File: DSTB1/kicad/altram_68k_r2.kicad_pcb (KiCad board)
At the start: 2 copper layers, 28.2 x 82 mm, 37 parts, among them IC1 IS42S16320D-7TL, IC2 SN74CB3T3245PW, IC3 SN74CB3T3245PW, J1 Conn_01x06_Male, U1 68000D, U2 68000D, U3 XC95144XL-TQ100, U4 LT1129-3.3_SOT223, X1 IQXO-70

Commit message: Working on the refactor for rev2
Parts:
- removed JP1: SolderJumper_3_Open, Jumper:SolderJumper-3_P1.3mm_Open_RoundedPad1.0x1.5mm
- removed RN11: 3k3, Resistor_SMD:R_Array_Convex_4x0603
- added R3: 2k2, Resistor_SMD:R_0805_2012Metric_Pad1.20x1.40mm_HandSolder, B.Cu at (144.7, 130.1)
- J1: value Conn_01x06_Male -> Conn_01x06_Pin
- R1: value R -> 1k
- TP1, TP2: value TestPoint -> (none)
- moved C5 13.1 mm to (148.2, 93.1), turned to 90 degrees
- moved R1 4.51 mm to (146.2, 127.3), turned to -90 degrees
- moved D1 3.54 mm to (149.6, 130.7), turned to 180 degrees
- moved U1 2.54 mm to (134.1, 55.6)
- moved U2 2.54 mm to (131.6, 55.6)
- moved TP1 0.15 mm to (141.7, 130.1), turned to 0 degrees
- turned TP2 to 0 degrees
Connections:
- net /TP1 renamed /TOS206
- net R~W renamed R~{W}
- net ~AS renamed ~{AS}
- net ~AS_INT renamed ~{AS_INT}
- net ~BERR renamed ~{BERR}
- net ~BOE renamed ~{BOE}
- net ~CAS renamed ~{CAS}
- net ~DTACK renamed ~{DTACK}
- net ~DTACK_INT renamed ~{DTACK_INT}
- net ~HLT renamed ~{HLT}
- net ~LDS renamed ~{LDS}
- net ~RAMWE renamed ~{RAMWE}
- net ~RAS renamed ~{RAS}
- net ~RST renamed ~{RST}
- net ~UDS renamed ~{UDS}
- net ~VMA renamed ~{VMA}
- net ~VMA_INT renamed ~{VMA_INT}
- net ~VPA renamed ~{VPA}
- C7 pad 1: Net-(C7-Pad1) -> VCC3
- IC1 pad 37: VCC3 -> CKE
- IC1 pad 38: RAMCLK -> OSC
- IC1 pad 40: Net-(IC1-Pad40) -> unconnected-(IC1-NC-Pad40)
- IC2 pad 1: Net-(IC2-Pad1) -> unconnected-(IC2-NC-Pad1)
- IC3 pad 1: Net-(IC3-Pad1) -> unconnected-(IC3-NC-Pad1)
- RN10 pad 5: Net-(RN10-Pad5) -> unconnected-(RN10-R4.2-Pad5)
- U1 pad 11: BG -> BGO
- U2 pad 11: BG -> BGI
- U3 pad 15: Net-(U3-Pad15) -> unconnected-(U3-P15-Pad15)
- U3 pad 16: Net-(U3-Pad16) -> unconnected-(U3-P16-Pad16)
- U3 pad 24: Net-(U3-Pad24) -> unconnected-(U3-P24-Pad24)
- U3 pad 25: Net-(U3-Pad25) -> unconnected-(U3-P25-Pad25)
- U3 pad 27: RAMCLK -> OSC
- U3 pad 36: OSC -> unconnected-(U3-P36-Pad36)
- U3 pad 54: /TP4 -> BGO
- U3 pad 55: /TP5 -> BGI
- U3 pad 58: Net-(U3-Pad58) -> /TP4
- U3 pad 59: Net-(U3-Pad59) -> /TP5
- U3 pad 60: Net-(U3-Pad60) -> /TP3
- U3 pad 61: Net-(U3-Pad61) -> unconnected-(U3-P61-Pad61)
- U3 pad 65: Net-(U3-Pad65) -> unconnected-(U3-P65-Pad65)
- U3 pad 66: /TP3 -> CKE
- X1 pad 1: Net-(X1-Pad1) -> unconnected-(X1-E/B-Pad1)
- X1 pad 4: Net-(C7-Pad1) -> VCC3
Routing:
- net BGI: track 0.00 -> 46.3 mm, vias 0 -> 1
- net BGO: track 0.00 -> 42.8 mm, vias 0 -> 1
- net OSC: track 13.3 -> 52.5 mm, vias 2 -> 3
- net RAMCLK: track 38.6 -> 0.00 mm, vias 2 -> 0
- net CKE: track 0.00 -> 24.1 mm, vias 0 -> 2
- net VCC: track 212.9 -> 195.4 mm, vias 6 -> 4
- net VCC3: track 188.4 -> 173.2 mm
- net Net-(C7-Pad1): track 8.72 -> 0.00 mm, vias 1 -> 0
- net /TP3: track 37.2 -> 29.7 mm, vias 2 -> 1
- net Net-(D1-A): track 10.2 -> 3.28 mm
- net ~{DTACK_INT}: track 31.4 -> 37.1 mm
- net /TP2: track 33.0 -> 27.8 mm, vias 2 -> 1
- net ~{VMA_INT}: track 3.21 -> 7.67 mm
- net E_INT: track 3.02 -> 7.16 mm
- net E: track 5.76 -> 3.22 mm
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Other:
- net class CLK removed
- net class Default removed
- net class PWR removed
- board text added: "David’s ST Booster mk 1, DSTB1r2 Copyright 2021-4 D Henderson Released under the terms of the GPLv2 https://github.com/dh219/DSTB"
- board text added: "FRAME"
- board text added: "TOS206"
- board text added: "~{DSTB1}r2"
- board text removed: "David’s ST Booster mk 1, DSTB1r1 Copyright 2021-2 D Henderson & others Released under the terms of the GPLv2 https://github.com/dh219/DSTB"
- board text removed: "~DSTB1"

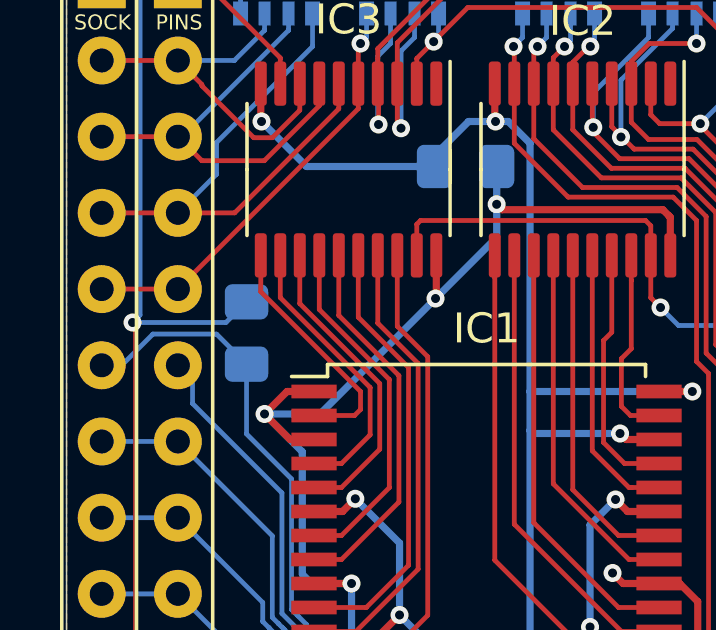
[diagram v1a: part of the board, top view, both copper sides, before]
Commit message: No DRC fails. All symbols updated. Bit of ground stitching.
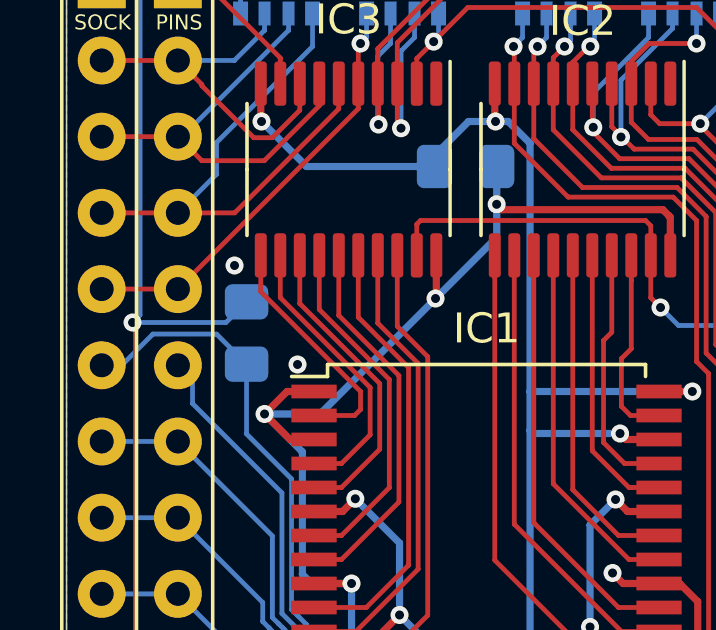
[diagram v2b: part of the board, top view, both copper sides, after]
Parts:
- TP1: value (none) -> TOS206
- TP2: value (none) -> FRAME
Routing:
- net GND: vias 27 -> 29
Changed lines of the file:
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@@
 			)
 		)
-		(property "Description" ""
+		(property "Description" "CPLD, 144 Macrocells, 3200 Usable Gates"
 			(at 0 0 0)
 			(layer "F.Fab")
@@
 			)
 		)
-		(property "Description" ""
+		(property "Description" "16/32-bit Microprocessor"
 			(at 0 0 0)
 			(layer "F.Fab")
@@
 			)
 		)
+		(property "Description_1" "Texas Instruments SN74CB3T3245DW, Bus Switch, 8 x 1:1, 2.3  3.6 V, 20-Pin SOIC"
+			(at 0 0 -90)
+			(unlocked yes)
+			(layer "F.Fab")
+			(hide yes)
+			(effects
+				(font
+					(size 1 1)
+					(thickness 0.15)
+				)
+			)
+		)
 		(sheetname "Root")
 		(sheetfile "altram_68k_r2.kicad_sch")
@@
 			)
 		)
+		(property "Description_1" "Texas Instruments SN74CB3T3245DW, Bus Switch, 8 x 1:1, 2.3  3.6 V, 20-Pin SOIC"
+			(at 0 0 -90)
+			(unlocked yes)
+			(layer "F.Fab")
+			(hide yes)
+			(effects
+				(font
+					(size 1 1)
+					(thickness 0.15)
+				)
+			)
+		)
 		(sheetname "Root")
 		(sheetfile "altram_68k_r2.kicad_sch")
@@
 			)
 		)
-		(property "Description" ""
+		(property "Description" "test point"
 			(at 0 0 90)
 			(layer "F.Fab")
@@
 			)
 		)
-		(property "Description" ""
+		(property "Description" "Crystal Clock Oscillator, SMD package 7.5x5.0mm²"
 			(at 0 0 -90)
 			(layer "F.Fab")
@@
 			)
 		)
-		(property "Description" ""
+		(property "Description" "test point"
 			(at 0 0 -90)
 			(layer "F.Fab")
@@
 			)
 		)
-		(property "Description" ""
+		(property "Description" "test point"
 			(at 0 0 -90)
 			(layer "F.Fab")
@@
 		(tags "LED handsolder")
 		(property "Reference" "D1"
-			(at 0 1.65 360)
+			(at 0 1.65 0)
 			(layer "F.SilkS")
 			(effects
@@
 		)
 		(property "Value" "LED"
-			(at 0 1.65 360)
+			(at 0 1.65 0)
 			(layer "F.Fab")
 			(effects
@@
 		)
 		(property "Footprint" "LED_SMD:LED_0805_2012Metric_Pad1.15x1.40mm_HandSolder"
-			(at 0 0 360)
+			(at 0 0 0)
 			(layer "F.Fab")
 			(hide yes)
@@
 		)
 		(property "Datasheet" ""
-			(at 0 0 360)
+			(at 0 0 0)
 			(layer "F.Fab")
 			(hide yes)
@@
 			)
 		)
-		(property "Description" ""
-			(at 0 0 360)
+		(property "Description" "Light emitting diode"
+			(at 0 0 0)
 			(layer "F.Fab")
 			(hide yes)
@@
 		)
 		(fp_text user "${REFERENCE}"
-			(at 0 0 360)
+			(at 0 0 0)
 			(layer "F.Fab")
 			(effects
@@
 			)
 		)
-		(property "Value" ""
+		(property "Value" "TOS206"
 			(at 0 0 0)
 			(unlocked yes)
@@
 			)
 		)
-		(property "Footprint" ""
+		(property "Footprint" "TestPoint:TestPoint_THTPad_1.0x1.0mm_Drill0.5mm"
 			(at 0 0 0)
 			(unlocked yes)
@@
 			)
 		)
+		(property "Datasheet" ""
+			(at 0 0 0)
+			(layer "F.Fab")
+			(hide yes)
+			(effects
+				(font
+					(size 1.27 1.27)
+					(thickness 0.15)
+				)
+			)
+		)
+		(property "Description" "test point"
+			(at 0 0 0)
+			(layer "F.Fab")
+			(hide yes)
+			(effects
+				(font
+					(size 1.27 1.27)
+					(thickness 0.15)
+				)
+			)
+		)
 		(property ki_fp_filters "Pin* Test*")
 		(sheetname "Root")
@@
 			)
 		)
-		(property "Value" ""
+		(property "Value" "FRAME"
 			(at 0 0 0)
 			(unlocked yes)
@@
 			)
 		)
-		(property "Footprint" ""
+		(property "Footprint" "TestPoint:TestPoint_THTPad_1.0x1.0mm_Drill0.5mm"
 			(at 0 0 0)
 			(unlocked yes)
@@
 			)
 		)
+		(property "Datasheet" ""
+			(at 0 0 0)
+			(layer "F.Fab")
+			(hide yes)
+			(effects
+				(font
+					(size 1.27 1.27)
+					(thickness 0.15)
+				)
+			)
+		)
+		(property "Description" "test point"
+			(at 0 0 0)
+			(layer "F.Fab")
+			(hide yes)
+			(effects
+				(font
+					(size 1.27 1.27)
+					(thickness 0.15)
+				)
+			)
+		)
 		(property ki_fp_filters "Pin* Test*")
 		(sheetname "Root")
@@
 			)
 		)
-		(property "Description" ""
+		(property "Description" "4 resistor network, parallel topology"
 			(at 0 0 90)
 			(layer "F.Fab")
@@
 			)
 		)
-		(property ki_fp_filters "DIP* SOIC* R*Array*Concave* R*Array*Convex*")
+		(property ki_fp_filters "DIP* SOIC* R*Array*Concave* R*Array*Convex* MSOP*")
 		(sheetname "Root")
 		(sheetfile "altram_68k_r2.kicad_sch")
@@
 			)
 		)
-		(property "Description" ""
+		(property "Description" "Unpolarized capacitor"
 			(at 0 0 90)
 			(layer "F.Fab")
@@
 			)
 		)
-		(property "Description" ""
+		(property "Description" "Unpolarized capacitor"
 			(at 0 0 90)
 			(layer "F.Fab")
@@
 			)
 		)
-		(property "Description" ""
+		(property "Description" "Unpolarized capacitor"
 			(at 0 0 -90)
 			(layer "F.Fab")
@@
 			)
 		)
-		(property "Description" ""
+		(property "Description" "4 resistor network, parallel topology"
 			(at 0 0 0)
 			(layer "F.Fab")
@@
 			)
 		)
-		(property ki_fp_filters "DIP* SOIC* R*Array*Concave* R*Array*Convex*")
+		(property ki_fp_filters "DIP* SOIC* R*Array*Concave* R*Array*Convex* MSOP*")
 		(sheetname "Root")
 		(sheetfile "altram_68k_r2.kicad_sch")
@@
 			)
 		)
-		(property "Description" ""
+		(property "Description" "4 resistor network, parallel topology"
 			(at 0 0 0)
 			(layer "F.Fab")
@@
 			)
 		)
-		(property ki_fp_filters "DIP* SOIC* R*Array*Concave* R*Array*Convex*")
+		(property ki_fp_filters "DIP* SOIC* R*Array*Concave* R*Array*Convex* MSOP*")
 		(sheetname "Root")
 		(sheetfile "altram_68k_r2.kicad_sch")
@@
 			)
 		)
-		(property "Description" ""
+		(property "Description" "4 resistor network, parallel topology"
 			(at 0 0 0)
 			(layer "F.Fab")
@@
 			)
 		)
-		(property ki_fp_filters "DIP* SOIC* R*Array*Concave* R*Array*Convex*")
+		(property ki_fp_filters "DIP* SOIC* R*Array*Concave* R*Array*Convex* MSOP*")
 		(sheetname "Root")
 		(sheetfile "altram_68k_r2.kicad_sch")
@@
 			)
 		)
-		(property "Description" ""
+		(property "Description" "4 resistor network, parallel topology"
 			(at 0 0 180)
 			(layer "F.Fab")
@@
 			)
 		)
-		(property ki_fp_filters "DIP* SOIC* R*Array*Concave* R*Array*Convex*")
+		(property ki_fp_filters "DIP* SOIC* R*Array*Concave* R*Array*Convex* MSOP*")
 		(sheetname "Root")
 		(sheetfile "altram_68k_r2.kicad_sch")
@@
 			)
 		)
-		(property "Description" ""
+		(property "Description" "4 resistor network, parallel topology"
 			(at 0 0 90)
 			(layer "F.Fab")
@@
 			)
 		)
-		(property ki_fp_filters "DIP* SOIC* R*Array*Concave* R*Array*Convex*")
+		(property ki_fp_filters "DIP* SOIC* R*Array*Concave* R*Array*Convex* MSOP*")
 		(sheetname "Root")
 		(sheetfile "altram_68k_r2.kicad_sch")
@@
 			)
 		)
-		(property "Description" ""
+		(property "Description" "4 resistor network, parallel topology"
 			(at 0 0 90)
 			(layer "F.Fab")
@@
 			)
 		)
-		(property ki_fp_filters "DIP* SOIC* R*Array*Concave* R*Array*Convex*")
+		(property ki_fp_filters "DIP* SOIC* R*Array*Concave* R*Array*Convex* MSOP*")
 		(sheetname "Root")
 		(sheetfile "altram_68k_r2.kicad_sch")
@@
 			)
 		)
-		(property "Description" ""
+		(property "Description" "Unpolarized capacitor"
 			(at 0 0 0)
 			(layer "F.Fab")
@@
 			)
 		)
-		(property "Description" ""
+		(property "Description" "Unpolarized capacitor"
 			(at 0 0 180)
 			(layer "F.Fab")
@@
 			)
 		)
-		(property "Description" ""
+		(property "Description" "Unpolarized capacitor"
 			(at 0 0 90)
 			(layer "F.Fab")
@@
 			)
 		)
-		(property "Description" ""
+		(property "Description" "Unpolarized capacitor"
 			(at 0 0 90)
 			(layer "F.Fab")
@@
 			)
 		)
-		(property "Description" ""
+		(property "Description" "4 resistor network, parallel topology"
 			(at 0 0 0)
 			(layer "F.Fab")
@@
 			)
 		)
-		(property ki_fp_filters "DIP* SOIC* R*Array*Concave* R*Array*Convex*")
+		(property ki_fp_filters "DIP* SOIC* R*Array*Concave* R*Array*Convex* MSOP*")
 		(sheetname "Root")
 		(sheetfile "altram_68k_r2.kicad_sch")
@@
 			)
 		)
-		(property "Description" ""
+		(property "Description" "4 resistor network, parallel topology"
 			(at 0 0 0)
 			(layer "F.Fab")
@@
 			)
 		)
-		(property ki_fp_filters "DIP* SOIC* R*Array*Concave* R*Array*Convex*")
+		(property ki_fp_filters "DIP* SOIC* R*Array*Concave* R*Array*Convex* MSOP*")
 		(sheetname "Root")
 		(sheetfile "altram_68k_r2.kicad_sch")
@@
 			)
 		)
-		(property "Description" ""
+		(property "Description" "Resistor"
 			(at 0 0 -90)
 			(layer "F.Fab")
@@
 			)
 		)
-		(property "Description" ""
+		(property "Description" "700mA Micropower Low drop-out regulator, Fixed Output 3.3V, SOT-223"
 			(at 0 0 90)
 			(layer "F.Fab")
@@
 			)
 		)
-		(property "Description" ""
+		(property "Description" "Resistor"
 			(at 0 0 90)
 			(layer "F.Fab")
@@
 			)
 		)
-		(property "Description" ""
+		(property "Description" "4 resistor network, parallel topology"
 			(at 0 0 90)
 			(layer "F.Fab")
@@
 			)
 		)
-		(property ki_fp_filters "DIP* SOIC* R*Array*Concave* R*Array*Convex*")
+		(property ki_fp_filters "DIP* SOIC* R*Array*Concave* R*Array*Convex* MSOP*")
 		(sheetname "Root")
 		(sheetfile "altram_68k_r2.kicad_sch")
@@
 			)
 		)
-		(property "Description" ""
+		(property "Description" "Unpolarized capacitor"
 			(at 0 0 180)
 			(layer "F.Fab")
@@
 	)
 	(via
+		(at 138.1 68.3)
+		(size 0.6)
+		(drill 0.3)
+		(layers "F.Cu" "B.Cu")
+		(free yes)
+		(net 1)
+	)
+	(via
 		(at 146.7 80.8)
 		(size 0.6)
@@
 	)
 	(via
+		(at 136 65)
+		(size 0.6)
+		(drill 0.3)
+		(layers "F.Cu" "B.Cu")
+		(free yes)
+		(net 1)
+	)
+	(via
 		(at 141.9 80.8)
 		(size 0.6)
@@
 		(net_name "GND")
 		(layer "F.Cu")
-		(hatch edge 0.508)
+		(hatch edge 0.5)
+		(priority 1)
 		(connect_pads
 			(clearance 0.254)
 		)
-		(min_thickness 0.254)
+		(min_thickness 0.25)
 		(filled_areas_thickness no)
 		(fill yes
-			(thermal_gap 0.508)
-			(thermal_bridge_width 0.508)
+			(thermal_gap 0.5)
+			(thermal_bridge_width 0.5)
 		)
 		(polygon
 			(pts
-				(xy 158.6 136) (xy 130.4 136) (xy 130.4 54) (xy 158.6 54)
+				(xy 130.4 136) (xy 130.4 54) (xy 158.6 54) (xy 158.6 136)
 			)
 		)

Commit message: Adding an inline termination to the clk8 line, just in case.
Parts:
- added R4: 10R, Resistor_SMD:R_0805_2012Metric_Pad1.20x1.40mm_HandSolder, B.Cu at (137.5, 112.7)
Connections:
- U1 pad 15: CLK8 -> /CLK_ST
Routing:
- net /CLK_ST: track 0.00 -> 23.0 mm
- net CLK8: track 21.9 -> 7.16 mm

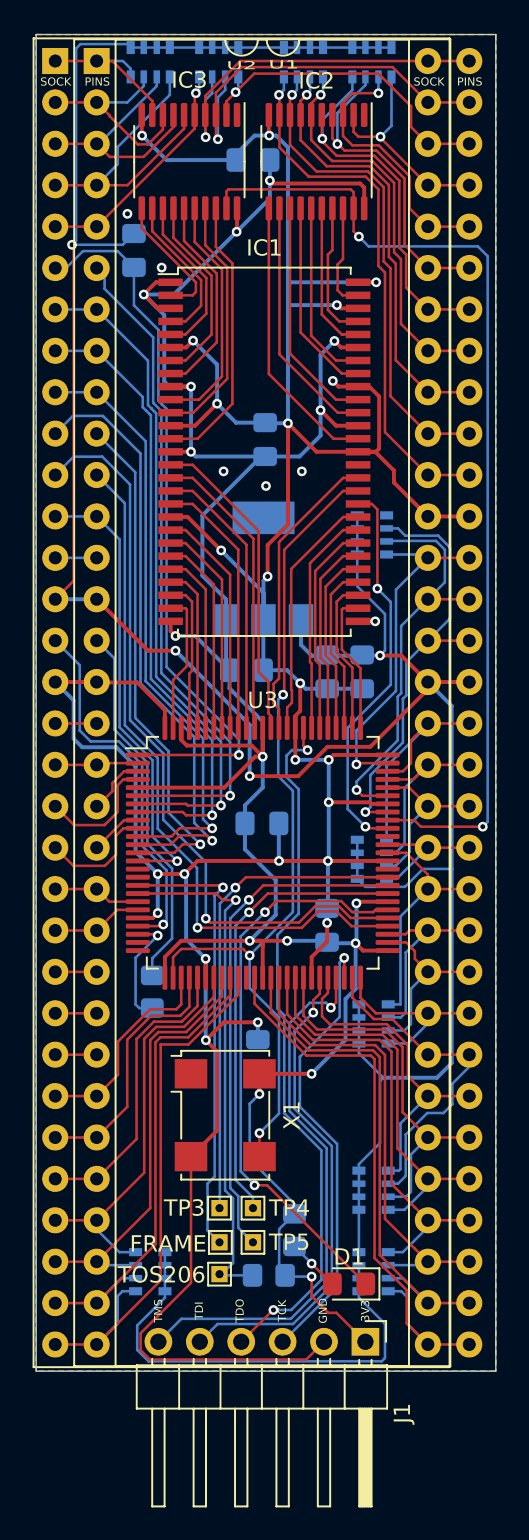
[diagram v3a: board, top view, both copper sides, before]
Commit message: Rejigged the bottom a bit to provide a better ground plane. Changed to the 1117-3.3 regulator
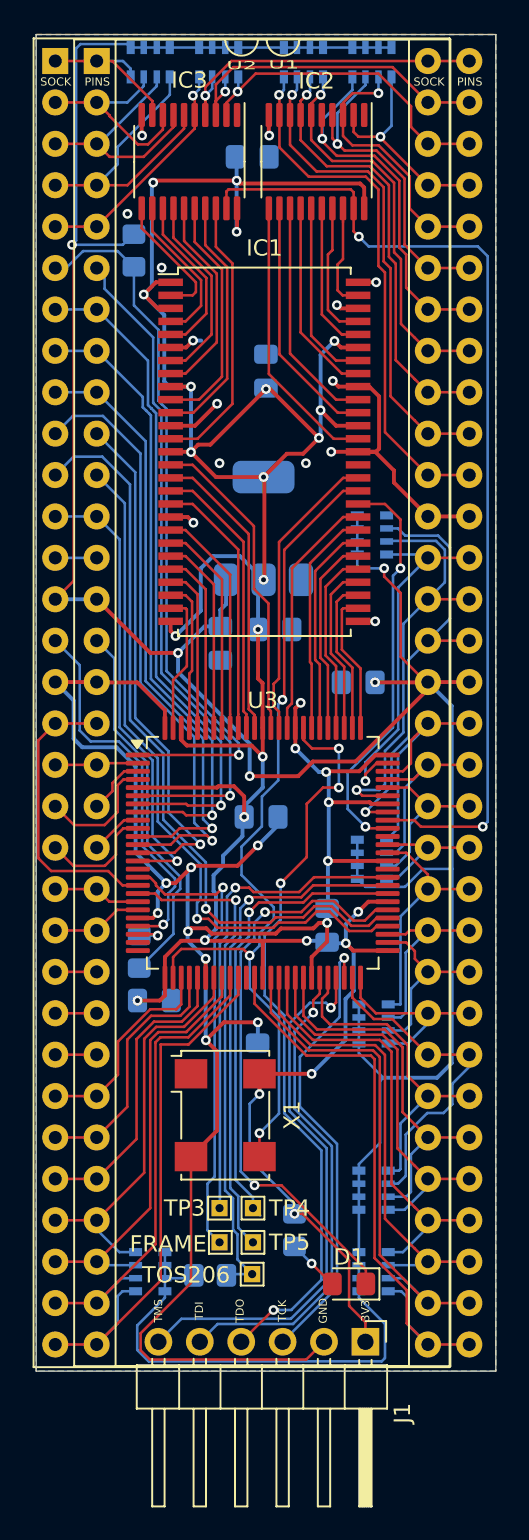
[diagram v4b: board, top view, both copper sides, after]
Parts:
- removed the C1 at (143.7, 61.7)
- removed C10: 10u, Capacitor_SMD:C_0805_2012Metric_Pad1.18x1.45mm_HandSolder
- added C2: 10u, Capacitor_SMD:C_0805_2012Metric_Pad1.18x1.45mm_HandSolder, B.Cu at (150.2, 93.7)
- added C6: 100n, Capacitor_SMD:C_0805_2012Metric_Pad1.18x1.45mm_HandSolder, B.Cu at (144.0, 116.9)
- added C8: 100n, Capacitor_SMD:C_0805_2012Metric_Pad1.18x1.45mm_HandSolder, B.Cu at (137.7, 113.3)
- C4: value 10u -> 100n
- R2: footprint Capacitor_SMD:C_0805_2012Metric_Pad1.18x1.45mm_HandSolder -> Resistor_SMD:R_0805_2012Metric_Pad1.20x1.40mm_HandSolder
- U4: value LT1129-3.3_SOT223 -> AMS1117-3.3
- moved C5 31.9 mm to (143.7, 61.5), turned to 0 degrees
- moved C4 19.4 mm to (144.5, 74.7)
- moved C7 14.7 mm to (144.2, 102.0), turned to 180 degrees
- moved C3 12.8 mm to (141.7, 91.3)
- moved R3 3.60 mm to (141.1, 130.1), turned to 180 degrees
- moved C1 3.05 mm to (145.1, 90.5)
- moved R4 2.58 mm to (136.7, 110.3), turned to -90 degrees
- moved U4 2.50 mm to (144.3, 84.3)
- moved TP1 2.00 mm to (143.7, 130.1)
- renumbered C8 to C1
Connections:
- C3 pad 1: VCC3 -> GND
- C3 pad 2: GND -> VCC
- C4 pad 1: GND -> VCC3
- C4 pad 2: VCC -> GND
- C5 pad 1: GND -> VCC3
- C5 pad 2: VCC -> GND
- C7 pad 1: VCC3 -> GND
- C7 pad 2: GND -> VCC3
- R3 pad 2: VCC3 -> VCC
- U3 pad 16: unconnected-(U3-P16-Pad16) -> /TP2
- U3 pad 17: /TP2 -> ~{HLT}
- U4 pad 1: VCC -> GND
- U4 pad 2: GND -> VCC3
- U4 pad 3: VCC3 -> VCC
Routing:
- net GND: track 232.3 -> 157.5 mm, vias 29 -> 28
- net VCC3: track 173.2 -> 192.2 mm, vias 16 -> 24
- net ~{HLT}: track 2.54 -> 18.0 mm
- net CLK8: track 7.16 -> 2.39 mm
- net VCC: track 195.4 -> 200.1 mm, vias 4 -> 5
- net D6: track 24.0 -> 21.3 mm
- net /TDO: track 43.5 -> 46.2 mm, vias 2 -> 4
- net D5: track 23.5 -> 21.1 mm
- net CKE: track 24.1 -> 25.0 mm
- net /LED1: track 35.2 -> 36.1 mm
- net A23: track 21.6 -> 22.5 mm
- net OSC: track 52.5 -> 53.3 mm
- net A22: track 25.4 -> 26.2 mm
- net /TP2: track 27.8 -> 28.6 mm
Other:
- board text added: "GND VOUT VIN"
- board text added: "REGULATOR NOT COMPATIBLE WITH DSTB1r1"
- board text removed: "VIN GND VOUT"
